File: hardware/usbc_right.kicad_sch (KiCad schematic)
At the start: 18 parts, among them J1 INPUT USB, U1 TPS259261, U2 AP2125N-3.3TRG1

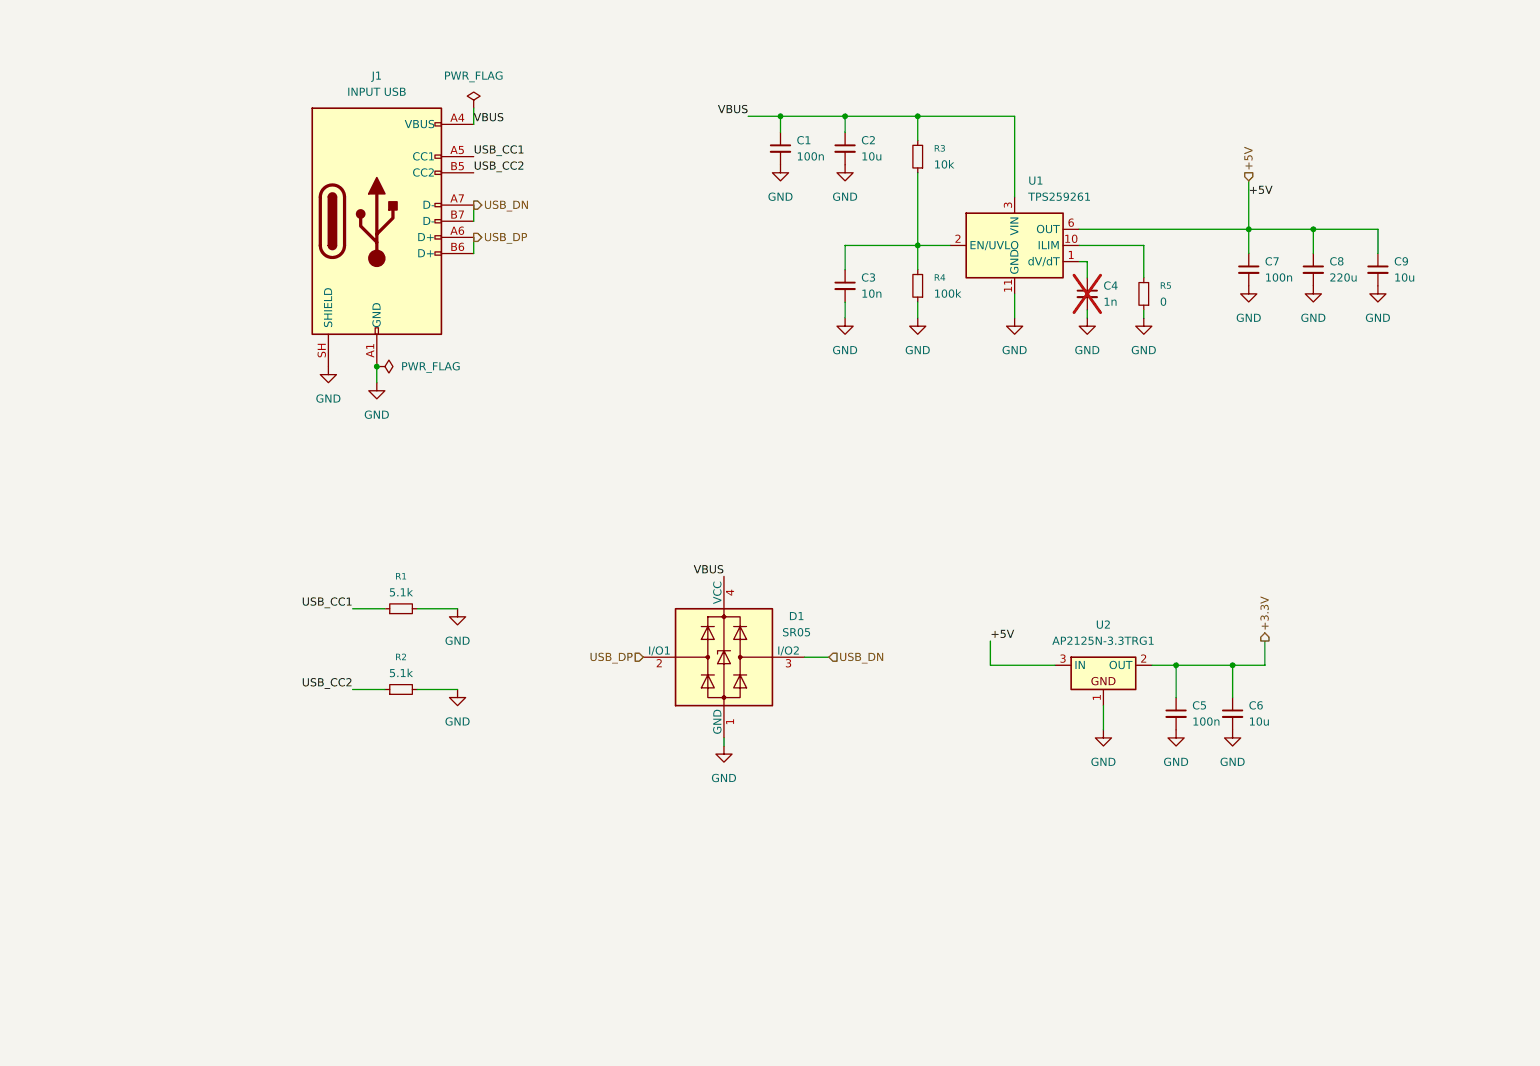
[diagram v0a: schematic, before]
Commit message: separate left/right part design, schematic
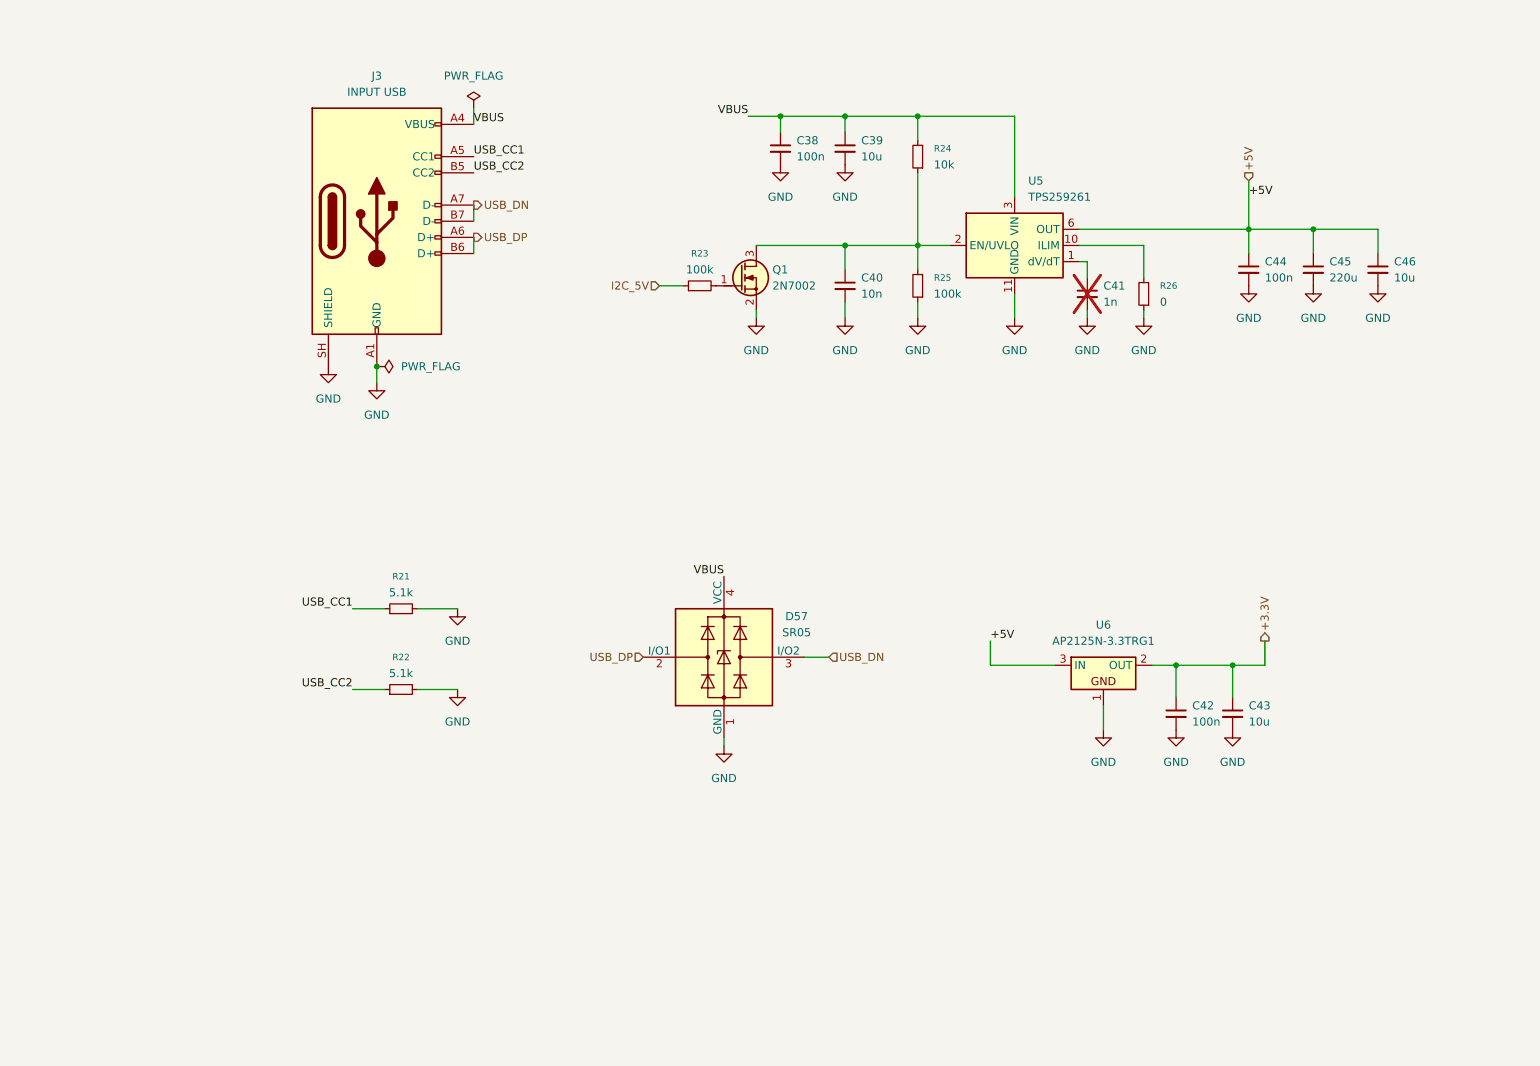
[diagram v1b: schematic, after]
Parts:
- removed C1, C5, C7: 100n, PCM_Capacitor_SMD_AKL:C_0603_1608Metric_Pad1.05x0.95mm_HandSolder, symbol Device:C_Small
- removed C2: 10u, PCM_Capacitor_SMD_AKL:C_0603_1608Metric_Pad1.05x0.95mm_HandSolder, symbol Device:C_Small
- removed C3: 10n, PCM_Capacitor_SMD_AKL:C_0603_1608Metric_Pad1.05x0.95mm_HandSolder, symbol Device:C_Small
- removed C4: 1n, PCM_Capacitor_SMD_AKL:C_0603_1608Metric_Pad1.05x0.95mm_HandSolder, symbol Device:C_Small
- removed C6, C9: 10u, PCM_Capacitor_SMD_AKL:C_0805_2012Metric_Pad1.15x1.40mm_HandSolder, symbol Device:C_Small
- removed C8: 220u, PCM_Capacitor_SMD_AKL:C_1210_3225Metric_Pad1.33x2.70mm_HandSolder, symbol Device:C_Small
- removed D1: SR05, Package_TO_SOT_SMD:SOT-143, symbol Power_Protection:PRTR5V0U2X
- removed J1: INPUT USB, Connector_USB:USB_C_Receptacle_GCT_USB4105-xx-A_16P_TopMnt_Horizontal, symbol Connector:USB_C_Receptacle_USB2.0_14P
- removed R1, R2: 5.1k, PCM_Resistor_SMD_AKL:R_0603_1608Metric_Pad0.98x0.95mm_HandSolder, symbol Device:R_Small
- removed R3: 10k, PCM_Resistor_SMD_AKL:R_0603_1608Metric, symbol Device:R_Small
- removed R4: 100k, PCM_Resistor_SMD_AKL:R_0603_1608Metric, symbol Device:R_Small
- removed R5: 0, PCM_Resistor_SMD_AKL:R_0603_1608Metric_Pad0.98x0.95mm_HandSolder, symbol Device:R_Small
- removed U1: TPS259261, Package_SON:VSON-10-1EP_3x3mm_P0.5mm_EP1.65x2.4mm_ThermalVias, symbol Power_Management:TPS2592xx
- removed U2: AP2125N-3.3TRG1, PCM_Package_TO_SOT_SMD_AKL:SOT-23, symbol PCM_Voltage_Regulator_AKL:AP2125N-3.3TRG1
- added C38, C42, C44: 100n, PCM_Capacitor_SMD_AKL:C_0603_1608Metric_Pad1.05x0.95mm_HandSolder, symbol Device:C_Small
- added C39: 10u, PCM_Capacitor_SMD_AKL:C_0603_1608Metric_Pad1.05x0.95mm_HandSolder, symbol Device:C_Small
- added C40: 10n, PCM_Capacitor_SMD_AKL:C_0603_1608Metric_Pad1.05x0.95mm_HandSolder, symbol Device:C_Small
- added C41: 1n, PCM_Capacitor_SMD_AKL:C_0603_1608Metric_Pad1.05x0.95mm_HandSolder, symbol Device:C_Small
- added C43, C46: 10u, PCM_Capacitor_SMD_AKL:C_0805_2012Metric_Pad1.15x1.40mm_HandSolder, symbol Device:C_Small
- added C45: 220u, PCM_Capacitor_SMD_AKL:C_1210_3225Metric_Pad1.33x2.70mm_HandSolder, symbol Device:C_Small
- added D57: SR05, Package_TO_SOT_SMD:SOT-143, symbol Power_Protection:PRTR5V0U2X
- added J3: INPUT USB, Connector_USB:USB_C_Receptacle_GCT_USB4105-xx-A_16P_TopMnt_Horizontal, symbol Connector:USB_C_Receptacle_USB2.0_14P
- added Q1: 2N7002, PCM_Package_TO_SOT_SMD_AKL:SOT-23, symbol PCM_Transistor_MOSFET_AKL:2N7002K
- added R21, R22: 5.1k, PCM_Resistor_SMD_AKL:R_0603_1608Metric_Pad0.98x0.95mm_HandSolder, symbol Device:R_Small
- added R23: 100k, PCM_Resistor_SMD_AKL:R_0805_2012Metric_Pad1.15x1.40mm_HandSolder, symbol Device:R_Small
- added R24: 10k, PCM_Resistor_SMD_AKL:R_0603_1608Metric, symbol Device:R_Small
- added R25: 100k, PCM_Resistor_SMD_AKL:R_0603_1608Metric, symbol Device:R_Small
- added R26: 0, PCM_Resistor_SMD_AKL:R_0603_1608Metric_Pad0.98x0.95mm_HandSolder, symbol Device:R_Small
- added U5: TPS259261, Package_SON:VSON-10-1EP_3x3mm_P0.5mm_EP1.65x2.4mm_ThermalVias, symbol Power_Management:TPS2592xx
- added U6: AP2125N-3.3TRG1, PCM_Package_TO_SOT_SMD_AKL:SOT-23, symbol PCM_Voltage_Regulator_AKL:AP2125N-3.3TRG1
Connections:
- net +3.3V: now also C42.1, C43.1, U6.2 (OUT)
- net +5V: now also C44.1, C45.1, C46.1, U5.6 (OUT), U5.7 (OUT), U5.8 (OUT), U6.3 (IN)
- net GND: now also C38.2, C39.2, C40.2, C41.2, C42.2, C43.2, C44.2, C45.2, C46.2, D57.1 (GND), J3.A1 (GND), J3.A12 (GND), J3.B1 (GND), J3.B12 (GND), J3.SH (SHIELD), Q1.2 (S), R21.2, R22.2, R25.1, R26.1, U5.11 (GND), U6.1
- net USB_CC1: now also J3.A5 (CC1), R21.1
- net USB_CC2: now also J3.B5 (CC2), R22.1
- net USB_DN: now also D57.3 (I/O2), J3.A7 (D-), J3.B7 (D-)
- net USB_DP: now also D57.2 (I/O1), J3.A6 (D+), J3.B6 (D+)
- net VBUS: now also C38.1, C39.1, D57.4 (VCC), J3.A4 (VBUS), J3.A9 (VBUS), J3.B4 (VBUS), J3.B9 (VBUS), R24.2, U5.3 (VIN), U5.4 (VIN), U5.5 (VIN)
- new net: C40.1, Q1.3 (D), R24.1, R25.2, U5.2 (EN/UVLO)
- new net: R26.2, U5.10 (ILIM)
- new net: C41.1, U5.1 (dV/dT)
- new net: Q1.1 (G), R23.2
- new net I2C_5V: R23.1

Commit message: encoder to schematic
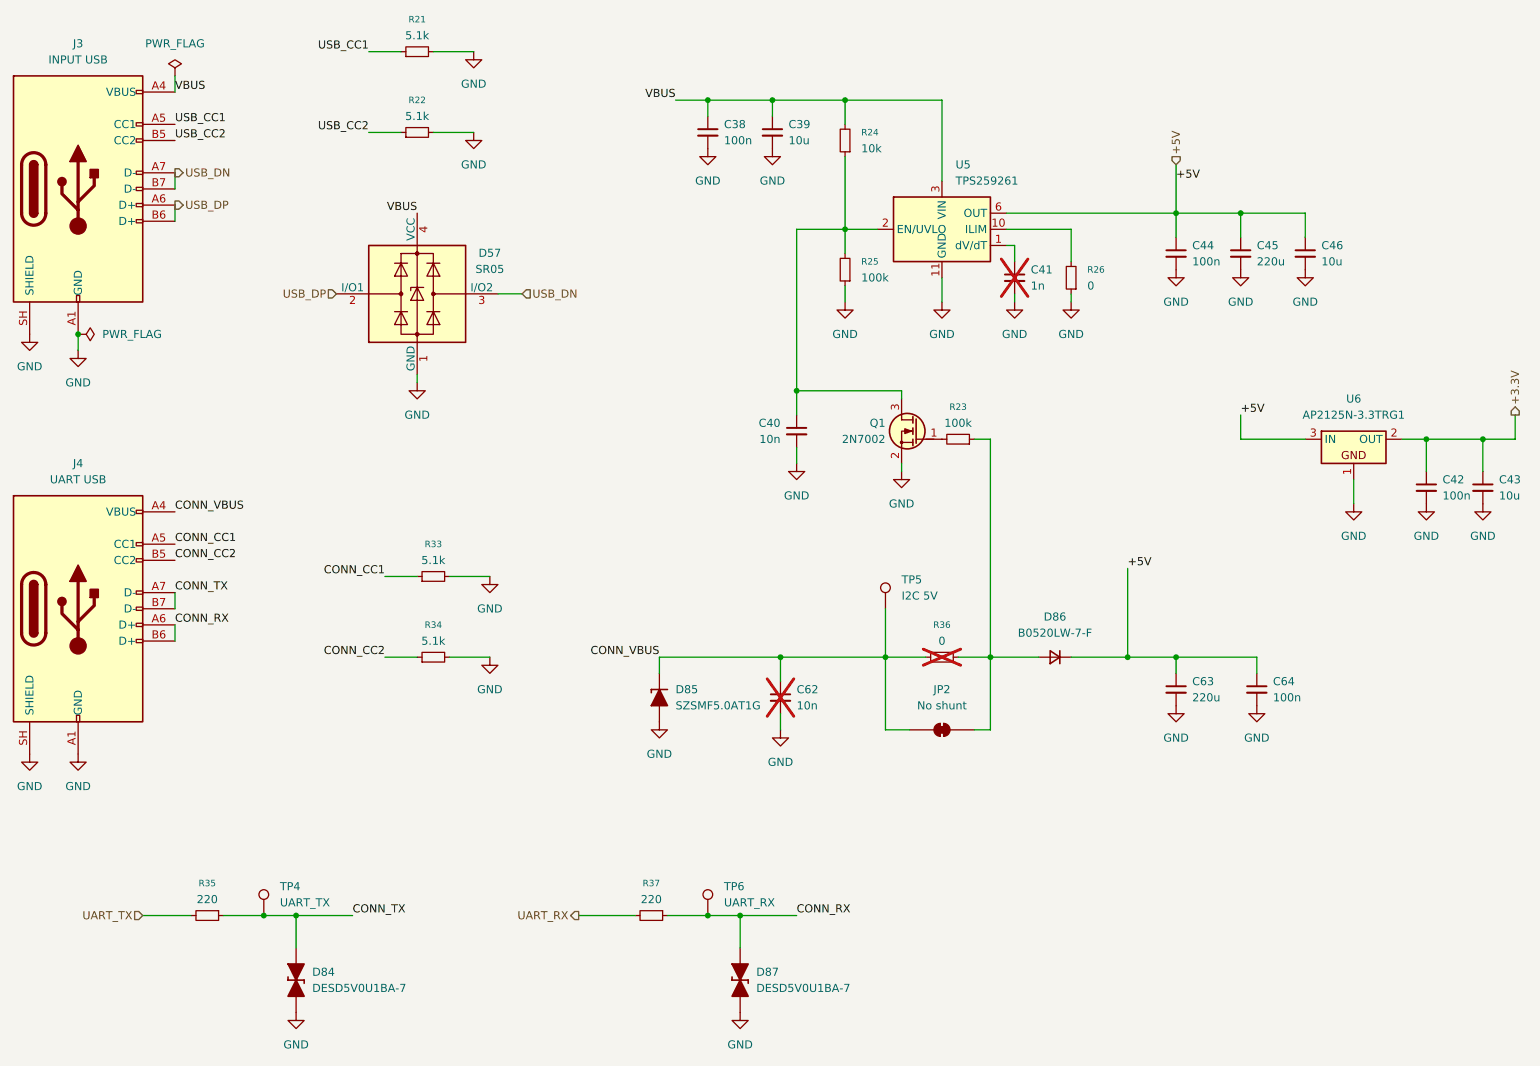
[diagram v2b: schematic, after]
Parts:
- added C62: 10n, PCM_Capacitor_SMD_AKL:C_0603_1608Metric_Pad1.05x0.95mm_HandSolder, symbol Device:C_Small
- added C63: 220u, PCM_Capacitor_SMD_AKL:C_1210_3225Metric_Pad1.33x2.70mm_HandSolder, symbol Device:C_Small
- added C64: 100n, PCM_Capacitor_SMD_AKL:C_0603_1608Metric, symbol Device:C_Small
- added D84, D87: DESD5V0U1BA-7, PCM_Diode_SMD_AKL:D_SOD-323_HandSoldering, symbol PCM_Diode_TVS_AKL:D_TVS_Bidirectional_Generic
- added D85: SZSMF5.0AT1G, PCM_Diode_SMD_Handsoldering_AKL:D_SOD-123_TVS, symbol PCM_Diode_TVS_AKL:D_TVS_Unidirectional_Generic
- added D86: B0520LW-7-F, PCM_Diode_SMD_AKL:D_SOD-123, symbol Device:D_Small
- added J4: UART USB, Connector_USB:USB_C_Receptacle_GCT_USB4105-xx-A_16P_TopMnt_Horizontal, symbol Connector:USB_C_Receptacle_USB2.0_14P
- added JP2: No shunt, Jumper:SolderJumper-2_P1.3mm_Bridged_RoundedPad1.0x1.5mm, symbol Jumper:SolderJumper_2_Bridged
- added R33, R34: 5.1k, PCM_Resistor_SMD_AKL:R_0603_1608Metric_Pad0.98x0.95mm_HandSolder, symbol Device:R_Small
- added R35, R37: 220, PCM_Resistor_SMD_AKL:R_0603_1608Metric_Pad0.98x0.95mm_HandSolder, symbol Device:R_Small
- added R36: 0, PCM_Resistor_SMD_AKL:R_1206_3216Metric_Pad1.30x1.75mm_HandSolder, symbol Device:R_Small
- added TP4: UART_TX, TestPoint:TestPoint_Pad_D2.0mm, symbol Connector:TestPoint
- added TP5: I2C 5V, TestPoint:TestPoint_Pad_D2.0mm, symbol Connector:TestPoint
- added TP6: UART_RX, TestPoint:TestPoint_Pad_D2.0mm, symbol Connector:TestPoint
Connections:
- net +5V: now also C63.1, C64.1, D86.1 (K)
- net GND: now also C62.2, C63.2, C64.2, D84.1 (K), D85.2 (A), D87.1 (K), J4.A1 (GND), J4.A12 (GND), J4.B1 (GND), J4.B12 (GND), J4.SH (SHIELD), R33.2, R34.2
- net I2C_5V: no longer names the net of R23.1
- net I2C_5V: now also D86.2 (A), JP2.2 (B), R36.1
- new net CONN_CC1: J4.A5 (CC1), R33.1
- new net CONN_CC2: J4.B5 (CC2), R34.1
- new net CONN_RX: D87.2 (A), J4.A6 (D+), J4.B6 (D+), R37.1, TP6.1
- new net CONN_TX: D84.2 (A), J4.A7 (D-), J4.B7 (D-), R35.1, TP4.1
- new net CONN_VBUS: C62.1, D85.1 (K), J4.A4 (VBUS), J4.A9 (VBUS), J4.B4 (VBUS), J4.B9 (VBUS), JP2.1 (A), R36.2, TP5.1
- new net UART_RX: R37.2
- new net UART_TX: R35.2
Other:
- moved on the sheet: C38, C39, C41, C42, C43, C44, C45, C46, D57, J3, Q1, R21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

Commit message: electronics
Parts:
- removed C63: 220u, PCM_Capacitor_SMD_AKL:C_1210_3225Metric_Pad1.33x2.70mm_HandSolder, symbol Device:C_Small
- removed C64: 100n, PCM_Capacitor_SMD_AKL:C_0603_1608Metric, symbol Device:C_Small
- C38: footprint PCM_Capacitor_SMD_AKL:C_0603_1608Metric_Pad1.05x0.95mm_HandSolder -> PCM_Capacitor_SMD_Handsoldering_AKL:C_0603_1608Metric; Distributor Link 3 (none) -> https://www.hestore.hu/prod_10033461.html
- C39: footprint PCM_Capacitor_SMD_AKL:C_0603_1608Metric_Pad1.05x0.95mm_HandSolder -> PCM_Capacitor_SMD_Handsoldering_AKL:C_0603_1608Metric; Distributor Link 3 (none) -> https://www.hestore.hu/prod_10043666.html
- C40: renamed from C62; footprint PCM_Capacitor_SMD_AKL:C_0603_1608Metric_Pad1.05x0.95mm_HandSolder -> PCM_Capacitor_SMD_Handsoldering_AKL:C_0603_1608Metric
- C41: renamed from C40; footprint PCM_Capacitor_SMD_AKL:C_0603_1608Metric_Pad1.05x0.95mm_HandSolder -> PCM_Capacitor_SMD_Handsoldering_AKL:C_0603_1608Metric; Distributor Link 3 (none) -> https://www.hestore.hu/prod_10027791.html
- C42: renamed from C41; footprint PCM_Capacitor_SMD_AKL:C_0603_1608Metric_Pad1.05x0.95mm_HandSolder -> PCM_Capacitor_SMD_Handsoldering_AKL:C_0603_1608Metric
- C43: renamed from C44; footprint PCM_Capacitor_SMD_AKL:C_0603_1608Metric_Pad1.05x0.95mm_HandSolder -> PCM_Capacitor_SMD_Handsoldering_AKL:C_0603_1608Metric; Distributor Link 3 (none) -> https://www.hestore.hu/prod_10033461.html
- C44: renamed from C45; footprint PCM_Capacitor_SMD_AKL:C_1210_3225Metric_Pad1.33x2.70mm_HandSolder -> PCM_Capacitor_SMD_Handsoldering_AKL:C_1210_3225Metric; Distributor Link 1 (none) -> https://hu.mouser.com/ProductDetail/KYOCERA-AVX/TCJB227M006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
- C45: renamed from C46; footprint PCM_Capacitor_SMD_AKL:C_0805_2012Metric_Pad1.15x1.40mm_HandSolder -> PCM_Capacitor_SMD_Handsoldering_AKL:C_0805_2012Metric; Distributor Link 1 (none) -> https://hu.mouser.com/ProductDetail/KEMET/C0805C106M8RACAUT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
- C46: renamed from C42; footprint PCM_Capacitor_SMD_AKL:C_0603_1608Metric_Pad1.05x0.95mm_HandSolder -> PCM_Capacitor_SMD_Handsoldering_AKL:C_0603_1608Metric; Distributor Link 3 (none) -> https://www.hestore.hu/prod_10033461.html
- C47: renamed from C43; footprint PCM_Capacitor_SMD_AKL:C_0805_2012Metric_Pad1.15x1.40mm_HandSolder -> PCM_Capacitor_SMD_Handsoldering_AKL:C_0805_2012Metric; Distributor Link 1 (none) -> https://hu.mouser.com/ProductDetail/KEMET/C0805C106M8RACAUT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
- D58: renamed from D84; footprint PCM_Diode_SMD_AKL:D_SOD-323_HandSoldering -> PCM_Diode_SMD_Handsoldering_AKL:D_SOD-323_TVS
- D59: renamed from D57; value SR05 -> PRTR5V0U2X; Distributor Link 1 https://hu.mouser.com/ProductDetail/Micro-Commercial-Compon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 -> https://hu.mouser.com/ProductDetail/Nexperia/PRTR5V0U2X215?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
- D60: renamed from D85; footprint PCM_Diode_SMD_Handsoldering_AKL:D_SOD-123_TVS -> PCM_Diode_SMD_Handsoldering_AKL:D_SOD-123_Zener
- D61: renamed from D87; footprint PCM_Diode_SMD_AKL:D_SOD-323_HandSoldering -> PCM_Diode_SMD_Handsoldering_AKL:D_SOD-323_TVS
- D62: renamed from D86; footprint PCM_Diode_SMD_AKL:D_SOD-123 -> PCM_Diode_SMD_Handsoldering_AKL:D_SOD-123
- R21: renamed from R35; footprint PCM_Resistor_SMD_AKL:R_0603_1608Metric_Pad0.98x0.95mm_HandSolder -> PCM_Resistor_SMD_AKL:R_0603_1608Metric; Distributor Link 3 (none) -> https://www.hestore.hu/prod_10036836.html
- R22: renamed from R21; footprint PCM_Resistor_SMD_AKL:R_0603_1608Metric_Pad0.98x0.95mm_HandSolder -> PCM_Resistor_SMD_AKL:R_0603_1608Metric; Distributor Link 3 (none) -> https://www.hestore.hu/prod_10036539.html
- R23: renamed from R22; footprint PCM_Resistor_SMD_AKL:R_0603_1608Metric_Pad0.98x0.95mm_HandSolder -> PCM_Resistor_SMD_AKL:R_0603_1608Metric; Distributor Link 3 (none) -> https://www.hestore.hu/prod_10036539.html
- R24: renamed from R33; footprint PCM_Resistor_SMD_AKL:R_0603_1608Metric_Pad0.98x0.95mm_HandSolder -> PCM_Resistor_SMD_AKL:R_0603_1608Metric; Distributor Link 3 (none) -> https://www.hestore.hu/prod_10036539.html
- R25: renamed from R34; footprint PCM_Resistor_SMD_AKL:R_0603_1608Metric_Pad0.98x0.95mm_HandSolder -> PCM_Resistor_SMD_AKL:R_0603_1608Metric; Distributor Link 3 (none) -> https://www.hestore.hu/prod_10036539.html
- R26: renamed from R37; footprint PCM_Resistor_SMD_AKL:R_0603_1608Metric_Pad0.98x0.95mm_HandSolder -> PCM_Resistor_SMD_AKL:R_0603_1608Metric; Distributor Link 3 (none) -> https://www.hestore.hu/prod_10036836.html
- R27: renamed from R24; Distributor Link 3 (none) -> https://www.hestore.hu/prod_10023910.html
- R28: renamed from R25; Distributor Link 3 (none) -> https://www.hestore.hu/prod_10043366.html
- R29: renamed from R36; footprint PCM_Resistor_SMD_AKL:R_1206_3216Metric_Pad1.30x1.75mm_HandSolder -> PCM_Resistor_SMD_AKL:R_1206_3216Metric
- R30: renamed from R23; footprint PCM_Resistor_SMD_AKL:R_0805_2012Metric_Pad1.15x1.40mm_HandSolder -> PCM_Resistor_SMD_AKL:R_0603_1608Metric; Distributor Link 3 (none) -> https://www.hestore.hu/prod_10043366.html
- R31: renamed from R26; footprint PCM_Resistor_SMD_AKL:R_0603_1608Metric_Pad0.98x0.95mm_HandSolder -> PCM_Resistor_SMD_AKL:R_0603_1608Metric; Distributor Link 3 (none) -> https://www.hestore.hu/prod_10043634.html
- renumbered TP6 to TP5, TP5 to TP6
